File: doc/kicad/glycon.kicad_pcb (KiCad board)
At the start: 4 copper layers, 114.3 x 80 mm, 15 parts, among them J1 2x20 Header, J2 USB_B, SW1 SW_Push, U0 Z80CPU, U1 628128_DIP32_SSOP32, U2 SST39SF010, U3 7432, X1 ACO-6.00MHz

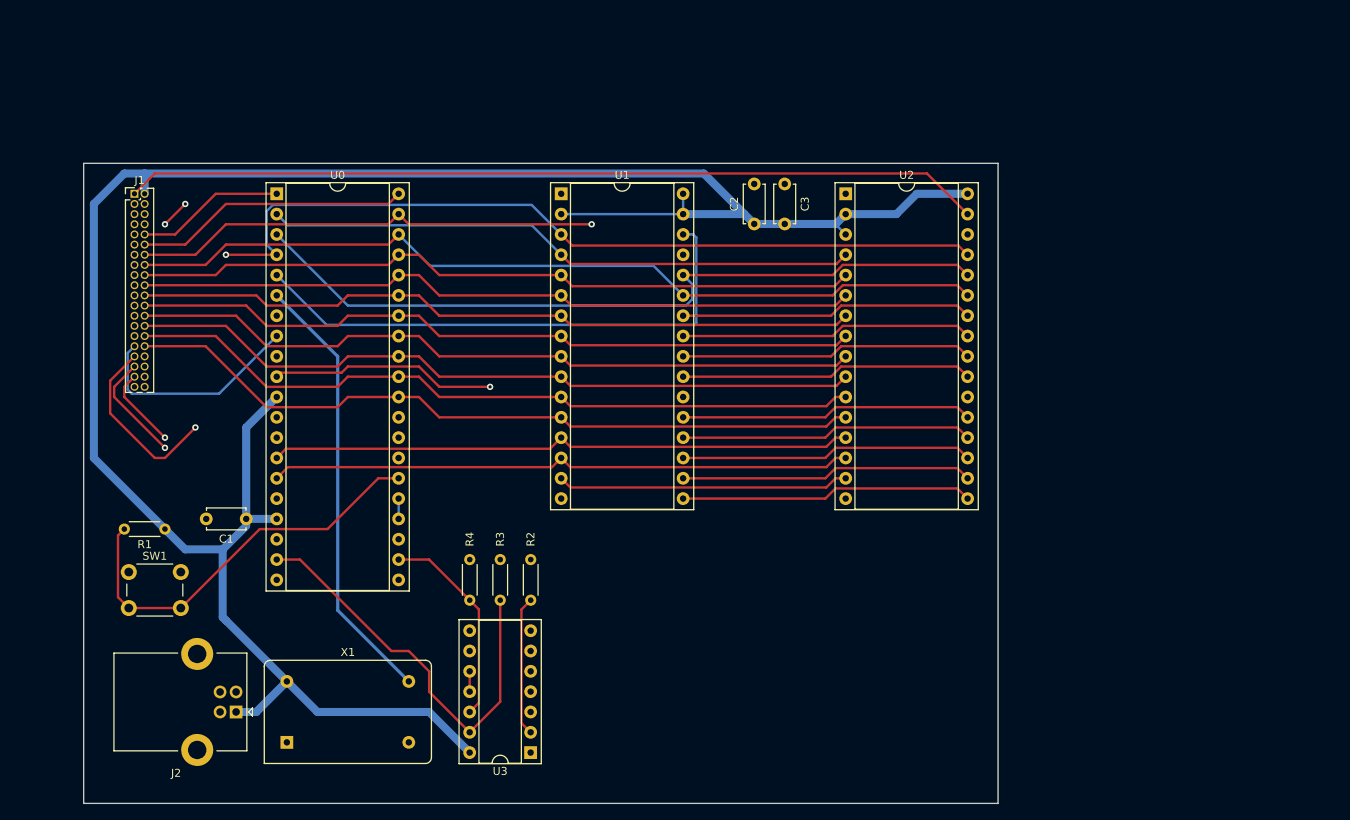
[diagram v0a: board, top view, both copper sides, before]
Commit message: add xor gates between coproc header and OE, ROM WE
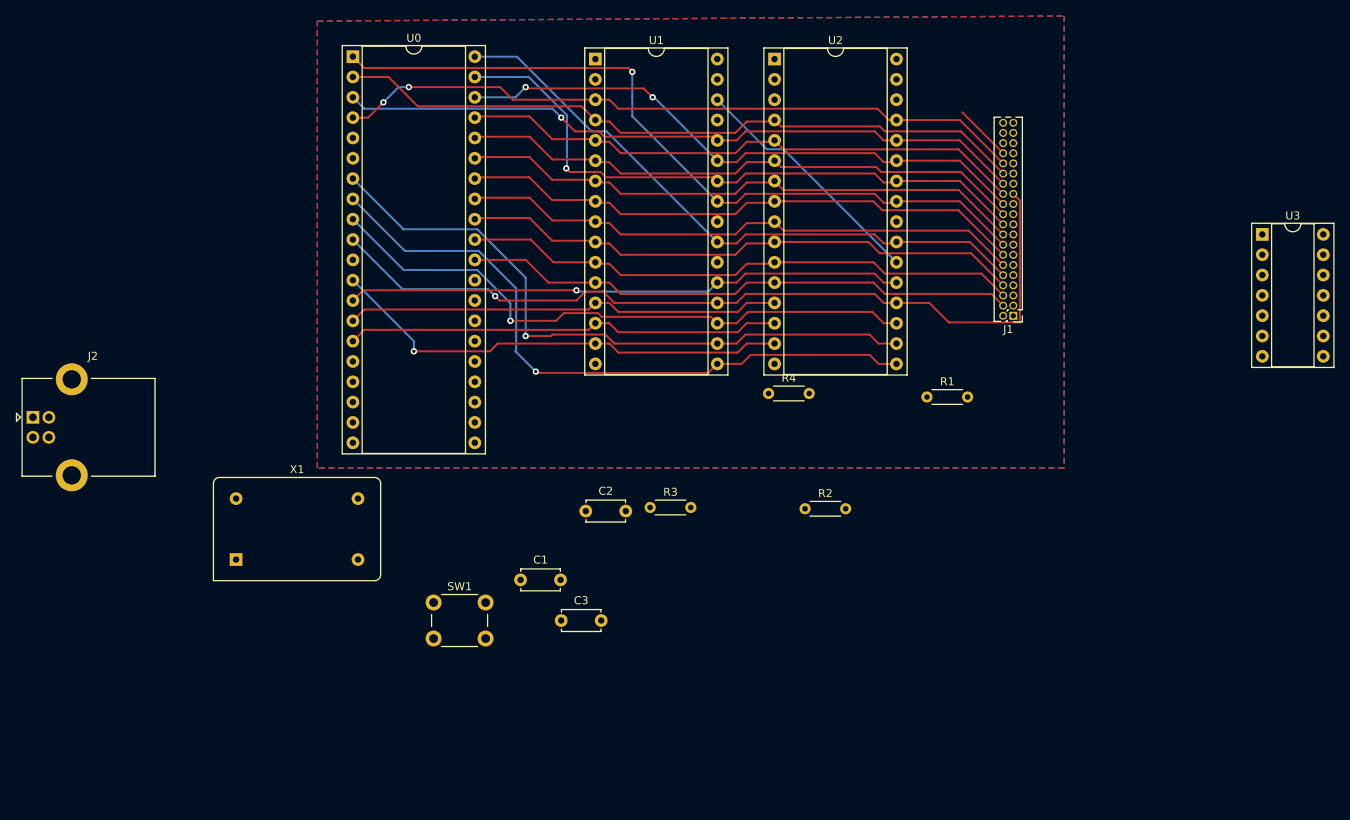
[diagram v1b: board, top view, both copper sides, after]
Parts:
- moved U3 112.1 mm to (191.8, 78.7), turned to 0 degrees
- moved J1 110.9 mm to (160.7, 88.9), turned to 180 degrees
- moved R1 96.7 mm to (149.9, 99.1), turned to 0 degrees
- moved C3 56.9 mm to (104.1, 127.0), turned to 0 degrees
- moved R4 45.4 mm to (130.1, 98.6), turned to 0 degrees
- moved J2 44.7 mm to (38.1, 101.6), turned to 0 degrees
- moved C2 41.6 mm to (107.2, 113.3), turned to 0 degrees
- moved SW1 38.3 mm to (88.2, 124.8)
- moved R2 36.1 mm to (134.6, 113.0), turned to 0 degrees
- moved C1 35.1 mm to (99.1, 121.9), turned to 0 degrees
- moved X1 23.7 mm to (63.5, 119.4)
- moved R3 22.0 mm to (115.3, 112.9), turned to 0 degrees
- moved U0 19.6 mm to (78.1, 56.5)
- moved U2 19.0 mm to (130.8, 56.8)
- moved U1 17.4 mm to (108.4, 56.8)
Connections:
- net Net-(J1-Pad34) renamed /A15
- J1 pad 10: /A11 -> /A10
- J1 pad 12: /A10 -> /A3
- J1 pad 14: /A9 -> /A4
- J1 pad 16: /A8 -> /A11
- J1 pad 18: /A7 -> /A5
- J1 pad 19: unconnected-(J1-Pad19) -> /RAM/ROM OE
- J1 pad 20: /A6 -> /A9
- J1 pad 22: /A5 -> /A6
- J1 pad 24: /A4 -> /A8
- J1 pad 26: /A3 -> /A7
- J1 pad 28: /A2 -> /A13
- J1 pad 30: /A1 -> /A12
- J1 pad 32: /A0 -> /A14
- J1 pad 4: /A14 -> /A0
- J1 pad 6: /A13 -> /A1
- J1 pad 8: /A12 -> /A2
- U0 pad 19: Net-(R3-Pad1) -> Net-(R4-Pad1)
- U0 pad 22: Net-(R4-Pad1) -> Net-(R3-Pad1)
- U1 pad 24: Net-(U1-Pad24) -> /RAM/ROM OE
- U2 pad 2: VCC -> Earth
- U2 pad 24: Net-(U1-Pad24) -> /RAM/ROM OE
- U2 pad 3: VCC -> Earth
- U3 pad 3: Net-(U1-Pad24) -> /RAM/ROM OE
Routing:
- net VCC: track 295.1 -> 0.00 mm
- net Earth: track 184.7 -> 0.00 mm
- net /ROM WE: track 107.3 -> 0.00 mm
- net /A15: track 132.3 -> 38.0 mm
- net Net-(U1-Pad24): track 91.5 -> 0.00 mm
- net Net-(U1-Pad29): track 84.8 -> 0.00 mm
- net /A10: track 152.9 -> 78.3 mm
- net /RAM WE: track 72.6 -> 0.00 mm
- net /D7: track 140.4 -> 69.9 mm, vias 0 -> 1
- net /D5: track 134.1 -> 76.6 mm, vias 0 -> 1
- net Net-(U0-Pad6): track 55.1 -> 0.00 mm
- net Net-(R3-Pad1): track 52.6 -> 0.00 mm
- net /D2: track 109.9 -> 58.5 mm
- net Net-(R1-Pad2): track 51.2 -> 0.00 mm
- net /D1: track 102.5 -> 54.6 mm, vias 1 -> 0
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- added copper zone on B.Cu, net Earth
- added copper zone on F.Cu, net VCC
- removed copper zone on In1.Cu, net Earth
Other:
- board outline removed
- copper layers 4 -> 2

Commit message: minor schematic updates
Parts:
- added R5: 10K, Resistor_THT:R_Axial_DIN0204_L3.6mm_D1.6mm_P5.08mm_Horizontal, F.Cu at (151.5, 119.4)
- added R6: 10K, Resistor_THT:R_Axial_DIN0204_L3.6mm_D1.6mm_P5.08mm_Horizontal, F.Cu at (142.9, 117.5)
- added R7: 10K, Resistor_THT:R_Axial_DIN0204_L3.6mm_D1.6mm_P5.08mm_Horizontal, F.Cu at (142.9, 120.7)
- added R8: 10K, Resistor_THT:R_Axial_DIN0204_L3.6mm_D1.6mm_P5.08mm_Horizontal, F.Cu at (142.9, 114.3)
- added R9: 10K, Resistor_THT:R_Axial_DIN0204_L3.6mm_D1.6mm_P5.08mm_Horizontal, F.Cu at (161.9, 97.8)
- added U4: 74HC86, Package_DIP:DIP-14_W7.62mm_Socket, F.Cu at (145.4, 102.9)
- R1: value 40K -> 10K
- R2, R3, R4: value 20K -> 10K
- U3: value 7432 -> 74HC32
- moved J2 113.2 mm to (151.1, 107.3)
- moved SW1 96.1 mm to (154.9, 55.5)
- moved U3 89.1 mm to (108.6, 110.5), turned to 90 degrees
- moved C3 77.6 mm to (142.8, 59.7), turned to 180 degrees
- moved C2 55.3 mm to (120.7, 59.7), turned to 180 degrees
- moved C1 41.8 mm to (83.2, 83.2)
- moved R1 39.5 mm to (113.7, 114.9)
- moved X1 31.9 mm to (94.6, 112.4), turned to 180 degrees
- moved R4 27.2 mm to (114.9, 121.3)
- moved R3 13.9 mm to (113.7, 99.1), turned to 180 degrees
- moved R2 2.62 mm to (135.3, 115.6)
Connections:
- C1 pad 1: VCC -> VDD
- C2 pad 1: VCC -> VDD
- C3 pad 1: VCC -> VDD
- J1 pad 2: VCC -> VDD
- J1 pad 36: unconnected-(J1-Pad36) -> Net-(J1-Pad36)
- J1 pad 38: unconnected-(J1-Pad38) -> Net-(J1-Pad38)
- J2 pad 1: VCC -> VDD
- R1 pad 1: VCC -> VDD
- R4 pad 1: Net-(R4-Pad1) -> Net-(R3-Pad1)
- U0 pad 11: VCC -> VDD
- U0 pad 16: unconnected-(U0-Pad16) -> VDD
- U0 pad 17: VCC -> VDD
- U0 pad 19: Net-(R4-Pad1) -> Net-(R3-Pad1)
- U0 pad 23: unconnected-(U0-Pad23) -> Net-(U0-Pad23)
- U0 pad 24: VCC -> VDD
- U0 pad 25: VCC -> Net-(J1-Pad36)
- U0 pad 5: /A15 -> Net-(R7-Pad2)
- U1 pad 2: VCC -> VDD
- U1 pad 24: /RAM/ROM OE -> Net-(U1-Pad24)
- U1 pad 30: /A15 -> Net-(U1-Pad30)
- U1 pad 31: VCC -> VDD
- U1 pad 32: VCC -> VDD
- U2 pad 22: /A15 -> Net-(U1-Pad30)
- U2 pad 24: /RAM/ROM OE -> Net-(U1-Pad24)
- U2 pad 31: /ROM WE -> Net-(U2-Pad31)
- U2 pad 32: VCC -> VDD
- U3 pad 1: Net-(R4-Pad1) -> Net-(R3-Pad1)
- U3 pad 12: Net-(R4-Pad1) -> Net-(R3-Pad1)
- U3 pad 14: VCC -> VDD
- U3 pad 3: /RAM/ROM OE -> Net-(U3-Pad3)
- U3 pad 4: (no net) -> Net-(R7-Pad2)
- U3 pad 5: (no net) -> /A15
- U3 pad 6: (no net) -> Net-(U1-Pad30)
- X1 pad 14: VCC -> VDD
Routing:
- net Net-(R1-Pad2): track 0.00 -> 113.9 mm, vias 0 -> 3
- net /D0: track 54.6 -> 127.8 mm, vias 0 -> 2
- net /D1: track 54.6 -> 122.0 mm, vias 0 -> 2
- net /D2: track 58.5 -> 116.8 mm, vias 1 -> 3
- net Net-(U0-Pad6): track 0.00 -> 55.1 mm
- net /D3: track 83.1 -> 125.8 mm
- net /D4: track 81.8 -> 119.9 mm
- net /A15: track 38.0 -> 0.00 mm
- net /D5: track 76.6 -> 112.3 mm
- net /D7: track 69.9 -> 102.9 mm, vias 1 -> 2
- net Net-(U1-Pad30): track 0.00 -> 30.8 mm
- net Earth: track 0.00 -> 15.3 mm
- net VDD: track 0.00 -> 14.2 mm
- net /D6: track 105.9 -> 98.4 mm
- removed copper zone on B.Cu, net Earth
- removed copper zone on F.Cu, net VCC
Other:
- board outline added: 96.5 x 73 mm
